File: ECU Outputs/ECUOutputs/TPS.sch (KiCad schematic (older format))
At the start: 22 parts, among them Q6 Q_NPN_BCE, Q7 Q_NPN_BCE, Q8 Q_PNP_BCE

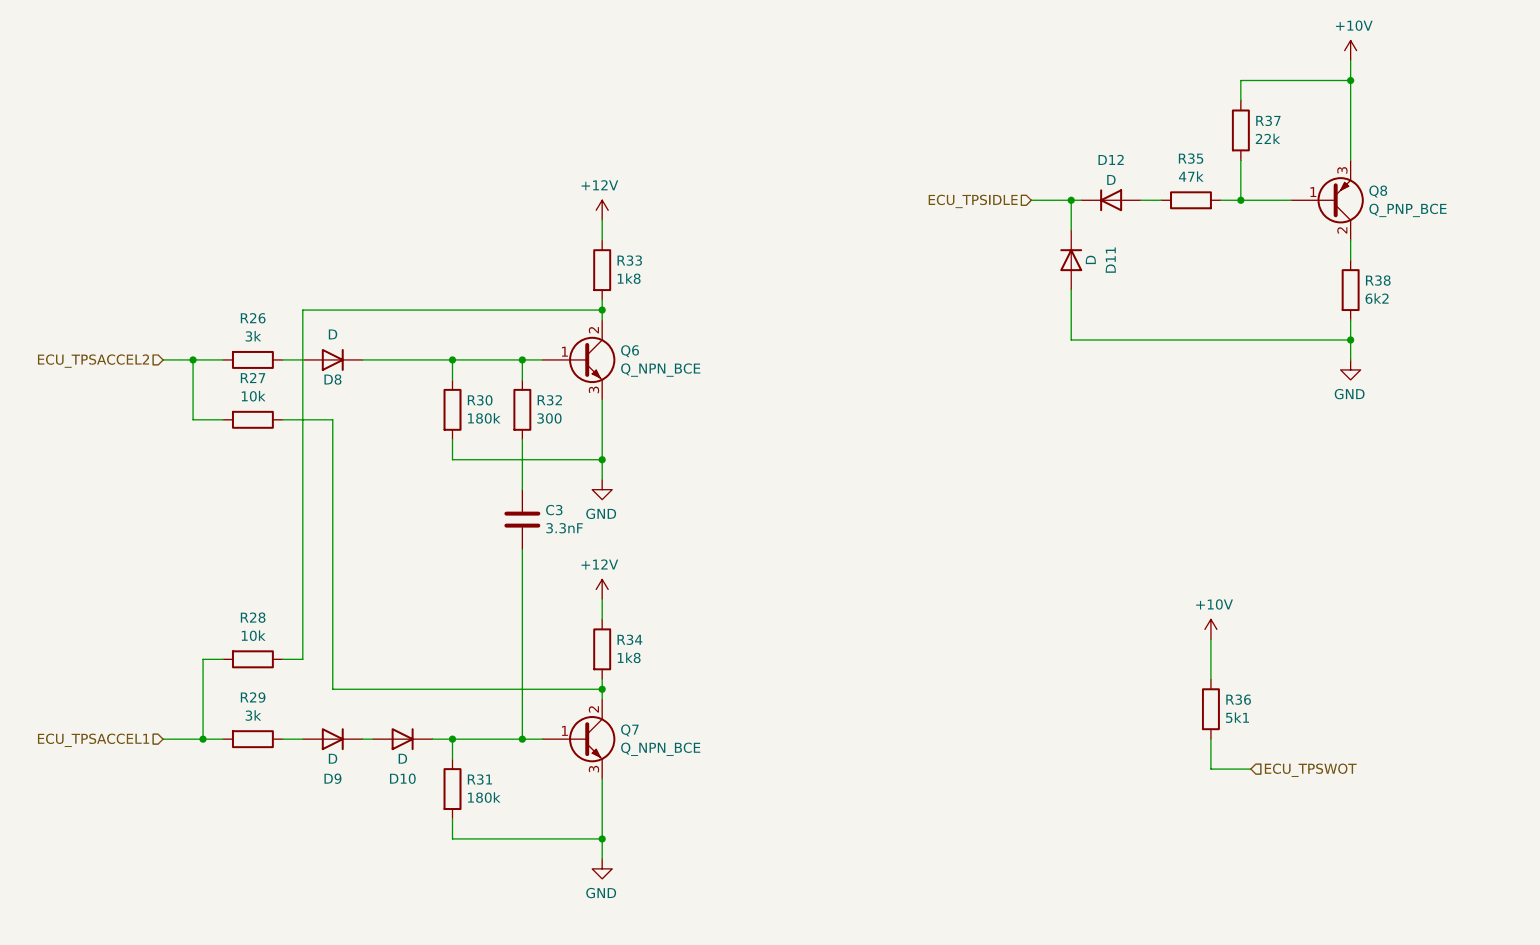
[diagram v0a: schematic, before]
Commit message: Corrected mistake in flip-flop copied from 005 ECU schematic.
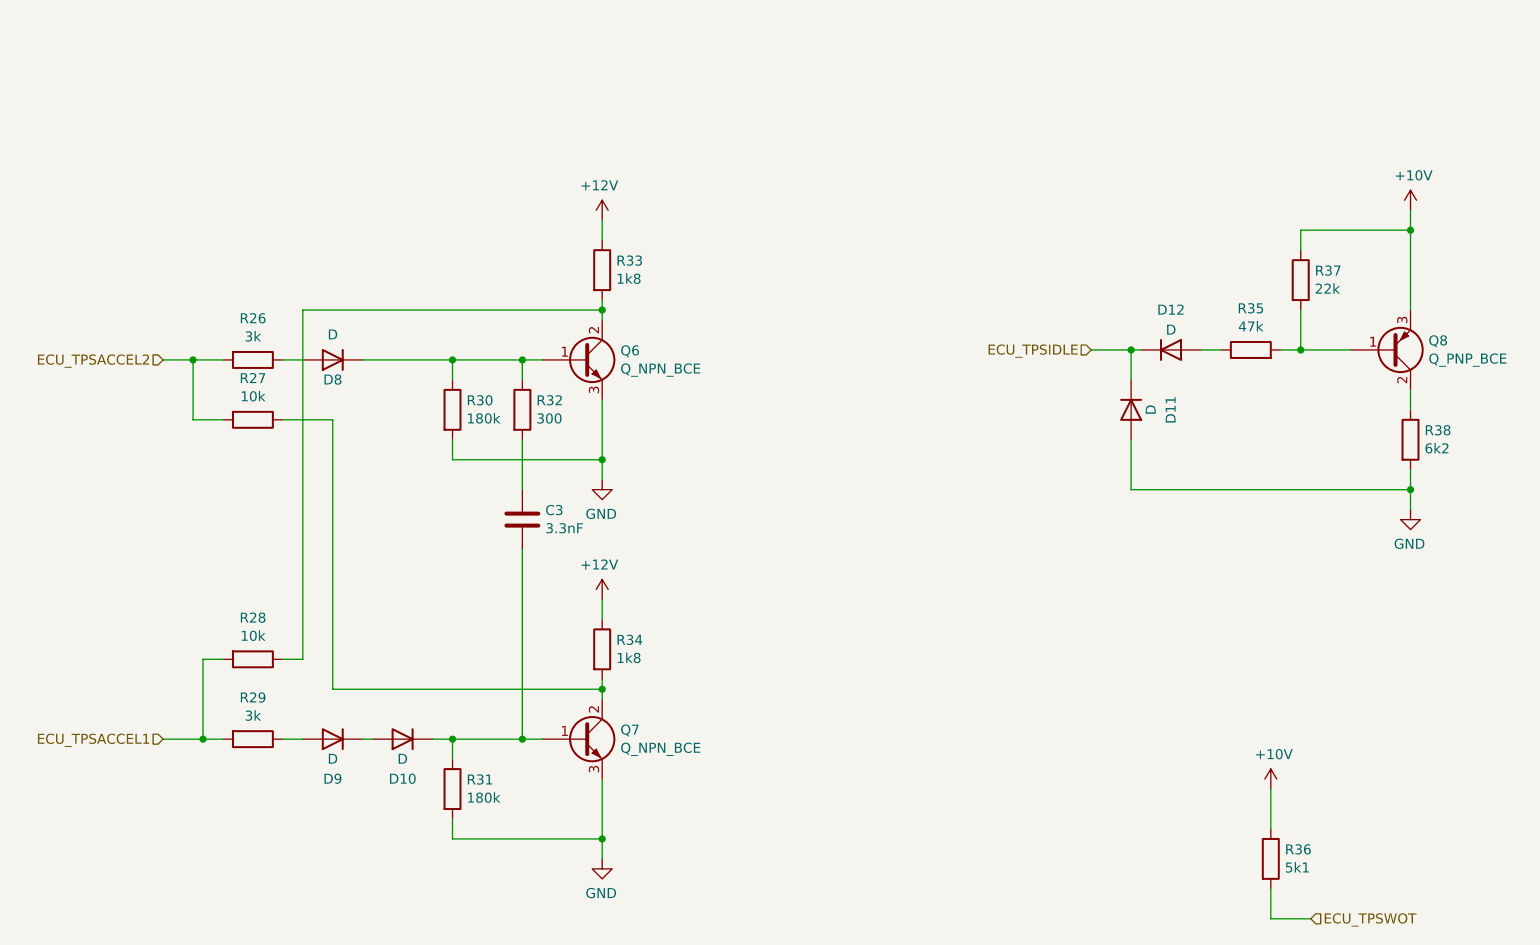
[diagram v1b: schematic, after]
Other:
- moved on the sheet: D11, D12, Q8, R35, R36, R37, R38
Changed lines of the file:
@@
 Sheet 3 3
 Title "ECU Outputs"
-Date "2021-03-07"
+Date "2021-03-10"
 Rev "1.0"
 Comp "Britishideas.com"
@@
 Wire Wire Line
 	3600 4700 3550 4700
-Text HLabel 6900 2000 0    50   Input ~ 0
+Text HLabel 7200 2750 0    50   Input ~ 0
 ECU_TPSIDLE
 $Comp
 L Device:D D?
 U 1 1 604CC7C0
-P 7300 2000
+P 7600 2750
 AR Path="/60469408/604CC7C0" Ref="D?"  Part="1"
 AR Path="/604A55C0/604CC7C0" Ref="D12"  Part="1"
-F 0 "D12" H 7300 2200 50  0000 C CNN
-F 1 "D" H 7300 2100 50  0000 C CNN
-F 2 "" H 7300 2000 50  0001 C CNN
-F 3 "~" H 7300 2000 50  0001 C CNN
-	1    7300 2000
+F 0 "D12" H 7600 2950 50  0000 C CNN
+F 1 "D" H 7600 2850 50  0000 C CNN
+F 2 "" H 7600 2750 50  0001 C CNN
+F 3 "~" H 7600 2750 50  0001 C CNN
+	1    7600 2750
 	1    0    0    -1
 $EndComp
@@
 L Device:R R?
 U 1 1 604CCFE1
-P 7700 2000
+P 8000 2750
 AR Path="/60469408/604CCFE1" Ref="R?"  Part="1"
 AR Path="/604A55C0/604CCFE1" Ref="R35"  Part="1"
-F 0 "R35" V 7907 2000 50  0000 C CNN
-F 1 "47k" V 7816 2000 50  0000 C CNN
-F 2 "" V 7630 2000 50  0001 C CNN
-F 3 "~" H 7700 2000 50  0001 C CNN
-	1    7700 2000
+F 0 "R35" V 8207 2750 50  0000 C CNN
+F 1 "47k" V 8116 2750 50  0000 C CNN
+F 2 "" V 7930 2750 50  0001 C CNN
+F 3 "~" H 8000 2750 50  0001 C CNN
+	1    8000 2750
 	0    -1   -1   0
 $EndComp
 Wire Wire Line
-	6900 2000 7100 2000
-Wire Wire Line
-	7450 2000 7550 2000
+	7200 2750 7400 2750
+Wire Wire Line
+	7750 2750 7850 2750
 $Comp
 L Device:Q_PNP_BCE Q8
 U 1 1 604CEFC7
-P 8400 2000
-F 0 "Q8" H 8590 1954 50  0000 L CNN
-F 1 "Q_PNP_BCE" H 8590 2045 50  0000 L CNN
-F 2 "" H 8600 2100 50  0001 C CNN
-F 3 "~" H 8400 2000 50  0001 C CNN
-	1    8400 2000
+P 8700 2750
+F 0 "Q8" H 8890 2704 50  0000 L CNN
+F 1 "Q_PNP_BCE" H 8890 2795 50  0000 L CNN
+F 2 "" H 8900 2850 50  0001 C CNN
+F 3 "~" H 8700 2750 50  0001 C CNN
+	1    8700 2750
 	1    0    0    1
 $EndComp
@@
 L Device:R R?
 U 1 1 604CFC45
-P 7950 1650
+P 8250 2400
 AR Path="/60469408/604CFC45" Ref="R?"  Part="1"
 AR Path="/604A55C0/604CFC45" Ref="R37"  Part="1"
-F 0 "R37" H 8020 1696 50  0000 L CNN
-F 1 "22k" H 8020 1605 50  0000 L CNN
-F 2 "" V 7880 1650 50  0001 C CNN
-F 3 "~" H 7950 1650 50  0001 C CNN
-	1    7950 1650
-	1    0    0    -1
-$EndComp
-Wire Wire Line
-	7850 2000 7950 2000
-Wire Wire Line
-	7950 1800 7950 2000
-Connection ~ 7950 2000
-Wire Wire Line
-	7950 2000 8200 2000
-Wire Wire Line
-	8500 1800 8500 1400
-Wire Wire Line
-	8500 1400 7950 1400
-Wire Wire Line
-	7950 1400 7950 1500
+F 0 "R37" H 8320 2446 50  0000 L CNN
+F 1 "22k" H 8320 2355 50  0000 L CNN
+F 2 "" V 8180 2400 50  0001 C CNN
+F 3 "~" H 8250 2400 50  0001 C CNN
+	1    8250 2400
+	1    0    0    -1
+$EndComp
+Wire Wire Line
+	8150 2750 8250 2750
+Wire Wire Line
+	8250 2550 8250 2750
+Connection ~ 8250 2750
+Wire Wire Line
+	8250 2750 8500 2750
+Wire Wire Line
+	8800 2550 8800 2150
+Wire Wire Line
+	8800 2150 8250 2150
+Wire Wire Line
+	8250 2150 8250 2250
 $Comp
 L power:+10V #PWR?
 U 1 1 604D2C70
-P 8500 1300
+P 8800 2050
 AR Path="/604D2C70" Ref="#PWR?"  Part="1"
 AR Path="/604A55C0/604D2C70" Ref="#PWR019"  Part="1"
-F 0 "#PWR019" H 8500 1150 50  0001 C CNN
-F 1 "+10V" H 8515 1473 50  0000 C CNN
-F 2 "" H 8500 1300 50  0001 C CNN
-F 3 "" H 8500 1300 50  0001 C CNN
-	1    8500 1300
-	1    0    0    -1
-$EndComp
-Wire Wire Line
-	8500 1300 8500 1400
-Connection ~ 8500 1400
+F 0 "#PWR019" H 8800 1900 50  0001 C CNN
+F 1 "+10V" H 8815 2223 50  0000 C CNN
+F 2 "" H 8800 2050 50  0001 C CNN
+F 3 "" H 8800 2050 50  0001 C CNN
+	1    8800 2050
+	1    0    0    -1
+$EndComp
+Wire Wire Line
+	8800 2050 8800 2150
+Connection ~ 8800 2150
 $Comp
 L Device:R R?
 U 1 1 604D4243
-P 8500 2450
+P 8800 3200
 AR Path="/60469408/604D4243" Ref="R?"  Part="1"
 AR Path="/604A55C0/604D4243" Ref="R38"  Part="1"
-F 0 "R38" H 8570 2496 50  0000 L CNN
-F 1 "6k2" H 8570 2405 50  0000 L CNN
-F 2 "" V 8430 2450 50  0001 C CNN
-F 3 "~" H 8500 2450 50  0001 C CNN
-	1    8500 2450
+F 0 "R38" H 8870 3246 50  0000 L CNN
+F 1 "6k2" H 8870 3155 50  0000 L CNN
+F 2 "" V 8730 3200 50  0001 C CNN
+F 3 "~" H 8800 3200 50  0001 C CNN
+	1    8800 3200
 	1    0    0    -1
 $EndComp
@@
 L Device:D D?
 U 1 1 604D47CA
-P 7100 2300
+P 7400 3050
 AR Path="/60469408/604D47CA" Ref="D?"  Part="1"
 AR Path="/604A55C0/604D47CA" Ref="D11"  Part="1"
-F 0 "D11" H 7100 2500 50  0000 C CNN
-F 1 "D" H 7100 2400 50  0000 C CNN
-F 2 "" H 7100 2300 50  0001 C CNN
-F 3 "~" H 7100 2300 50  0001 C CNN
-	1    7100 2300
+F 0 "D11" H 7400 3250 50  0000 C CNN
+F 1 "D" H 7400 3150 50  0000 C CNN
+F 2 "" H 7400 3050 50  0001 C CNN
+F 3 "~" H 7400 3050 50  0001 C CNN
+	1    7400 3050
 	0    1    1    0
 $EndComp
 Wire Wire Line
-	7100 2150 7100 2000
-Connection ~ 7100 2000
-Wire Wire Line
-	7100 2000 7150 2000
-Wire Wire Line
-	7100 2450 7100 2700
-Wire Wire Line
-	7100 2700 8500 2700
-Wire Wire Line
-	8500 2700 8500 2600
+	7400 2900 7400 2750
+Connection ~ 7400 2750
+Wire Wire Line
+	7400 2750 7450 2750
+Wire Wire Line
+	7400 3200 7400 3450
+Wire Wire Line
+	7400 3450 8800 3450
+Wire Wire Line
+	8800 3450 8800 3350
 $Comp
 L power:GND #PWR?
 U 1 1 604D6C3F
-P 8500 2800
+P 8800 3550
 AR Path="/604D6C3F" Ref="#PWR?"  Part="1"
 AR Path="/60479334/604D6C3F" Ref="#PWR?"  Part="1"
 AR Path="/60469408/604D6C3F" Ref="#PWR?"  Part="1"
 AR Path="/604A55C0/604D6C3F" Ref="#PWR020"  Part="1"
-F 0 "#PWR020" H 8500 2550 50  0001 C CNN
-F 1 "GND" H 8505 2627 50  0000 C CNN
-F 2 "" H 8500 2800 50  0001 C CNN
-F 3 "" H 8500 2800 50  0001 C CNN
-	1    8500 2800
+F 0 "#PWR020" H 8800 3300 50  0001 C CNN
+F 1 "GND" H 8805 3377 50  0000 C CNN
+F 2 "" H 8800 3550 50  0001 C CNN
+F 3 "" H 8800 3550 50  0001 C CNN
+	1    8800 3550
 	-1   0    0    -1
 $EndComp
 Wire Wire Line
-	8500 2800 8500 2700
-Connection ~ 8500 2700
-Wire Wire Line
-	8500 2300 8500 2200
-Text HLabel 8000 4850 2    50   Input ~ 0
+	8800 3550 8800 3450
+Connection ~ 8800 3450
+Wire Wire Line
+	8800 3050 8800 2950
+Text HLabel 8300 5600 2    50   Input ~ 0
 ECU_TPSWOT
 $Comp
 L Device:R R?
 U 1 1 604DCE0A
-P 7800 4550
+P 8100 5300
 AR Path="/60469408/604DCE0A" Ref="R?"  Part="1"
 AR Path="/604A55C0/604DCE0A" Ref="R36"  Part="1"
-F 0 "R36" H 7870 4596 50  0000 L CNN
-F 1 "5k1" H 7870 4505 50  0000 L CNN
-F 2 "" V 7730 4550 50  0001 C CNN
-F 3 "~" H 7800 4550 50  0001 C CNN
-	1    7800 4550
-	1    0    0    -1
-$EndComp
-Wire Wire Line
-	8000 4850 7800 4850
-Wire Wire Line
-	7800 4850 7800 4700
+F 0 "R36" H 8170 5346 50  0000 L CNN
+F 1 "5k1" H 8170 5255 50  0000 L CNN
+F 2 "" V 8030 5300 50  0001 C CNN
+F 3 "~" H 8100 5300 50  0001 C CNN
+	1    8100 5300
+	1    0    0    -1
+$EndComp
+Wire Wire Line
+	8300 5600 8100 5600
+Wire Wire Line
+	8100 5600 8100 5450
 $Comp
 L power:+10V #PWR?
 U 1 1 604DE272
-P 7800 4200
+P 8100 4950
 AR Path="/604DE272" Ref="#PWR?"  Part="1"
 AR Path="/604A55C0/604DE272" Ref="#PWR018"  Part="1"
-F 0 "#PWR018" H 7800 4050 50  0001 C CNN
-F 1 "+10V" H 7815 4373 50  0000 C CNN
-F 2 "" H 7800 4200 50  0001 C CNN
-F 3 "" H 7800 4200 50  0001 C CNN
-	1    7800 4200
-	1    0    0    -1
-$EndComp
-Wire Wire Line
-	7800 4200 7800 4400
+F 0 "#PWR018" H 8100 4800 50  0001 C CNN
+F 1 "+10V" H 8115 5123 50  0000 C CNN
+F 2 "" H 8100 4950 50  0001 C CNN
+F 3 "" H 8100 4950 50  0001 C CNN
+	1    8100 4950
+	1    0    0    -1
+$EndComp
+Wire Wire Line
+	8100 4950 8100 5150
 Wire Wire Line
 	3250 2550 3250 4300
